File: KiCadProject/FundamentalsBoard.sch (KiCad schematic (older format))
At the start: 17 parts

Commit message: updates
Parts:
- removed P? (x2): CONN_01X02, symbol CONN_01X02
- added C? (x3): 0.1 uF, symbol C
- added P? (x7): CONN_02X02, symbol CONN_02X02
- added P? (x3): CONN_01X03, symbol CONN_01X03
- added R? (x10): 5k, symbol R
- added R? (x3): 10k, symbol R
- added RV? (x2): 5k, symbol POT
- added RV? (x6): 10k, symbol POT
- added U? (x6): MCP601, symbol MCP601
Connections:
- net C_EmitterIn: now also P?.1 (P1), P?.2 (P2)
- net C_EmitterOut: now also P?.3 (P3), P?.4 (P4)
- net GND: now also C?.1, R?.1, R?.1, R?.1, R?.1, R?.2, RV?.3, U?.2 (V-), U?.2 (V-), U?.2 (V-), U?.2 (V-), U?.2 (V-), U?.2 (V-)
- net VCC: now also P?.1 (P1), P?.2 (P2), R?.1, RV?.1, U?.5 (V+), U?.5 (V+), U?.5 (V+), U?.5 (V+), U?.5 (V+), U?.5 (V+)
- net CMirror_n: now reaches Q?.1 (C)
- net CMirror_n: now also P?.3 (P3), P?.4 (P4)
- new net: P?.1 (P1), RV?.1 (x2)
- new net: P?.2 (P2), RV?.2 (x2)
- new net: P?.3 (P3), RV?.3 (x2)
- new net: R?.2, RV?.3, U?.3 (+)
- new net: RV?.2, U?.4 (-)
- new net: P?.1 (P1), P?.2 (P2), P?.3 (P3), R?.1, RV?.2, U?.1
- new net: R?.1, R?.2, U?.3 (+)
- new net: R?.2, R?.2, U?.4 (-)
- new net: C?.2, R?.2, RV?.1
- new net: R?.2, U?.3 (+) (x2)
- new net: C?.1, RV?.2, U?.4 (-)
- new net: C?.2, RV?.3, U?.4 (-)
- new net: R?.1, RV?.1, U?.3 (+)
- new net: R?.2, U?.4 (-)
- new net: R?.1, U?.3 (+)
- new net: R?.1, R?.1, R?.2, U?.4 (-)
- new net Amp_in: P?.1 (P1), P?.2 (P2), R?.2
- new net Amp_out: P?.3 (P3), P?.4 (P4), RV?.2, U?.1
- new net Diff_in: C?.1, P?.1 (P1), P?.2 (P2)
- new net Diff_out: P?.3 (P3), P?.4 (P4), RV?.2, U?.1
- new net Int_in: P?.1 (P1), P?.2 (P2), RV?.3
- new net Int_out: C?.2, P?.3 (P3), P?.4 (P4), U?.1
- new net STrigger_in: P?.1 (P1), P?.2 (P2), RV?.2
- new net STrigger_out: P?.3 (P3), P?.4 (P4), R?.1, U?.1
- new net V1add_in: P?.3 (P3), R?.2
- new net V2add_in: P?.1 (P1), R?.2
- new net Vadd_out: P?.2 (P2), P?.4 (P4), R?.1, U?.1
- no-connect marks 2 -> 7
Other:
- note added: "Amplifier"
- note added: "Differentiator\n"
- note added: "Extra 10k\nPotentiometer"
- note added: "Extra 5k\nPotentiometer"
- note added: "G=-Rf/Rin"
- note added: "Integrator\n"
- note added: "Osc. range:\n1kHz - inf"
- note added: "Schmitt Trigger"
- note added: "Schmitt Trigger\nBased Oscillator\n"
- note added: "Voltage Adder\n"

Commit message: Added Footprints
Added footprint types to most components
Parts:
- removed Q? (x3): BC550, TO-92, symbol BC550
- added D? (x3): LED, LEDs:LED_0603, symbol LED
- added P?: CONN_01X03, Pin_Headers:Pin_Header_Straight_1x03, symbol CONN_01X03
- added R? (x3): 470R, Resistors_SMD:R_0603, symbol R
- C21, C? (x2): footprint (none) -> Capacitors_SMD:C_0603
- C?: value 0.1 uF -> 1 uF; footprint (none) -> Capacitors_SMD:C_0603
- P? (x7): footprint (none) -> Pin_Headers:Pin_Header_Straight_2x02
- P? (x3): footprint (none) -> Pin_Headers:Pin_Header_Straight_1x03
- Q? (x3): footprint TO-92 -> TO_SOT_Packages_SMD:SOT-23
- R21, R22, R23, R24, R? (x15): footprint (none) -> Resistors_SMD:R_0603
- U? (x6): footprint (none) -> TO_SOT_Packages_SMD:SOT-23-5
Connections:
- net GND: now also D?.1 (K), D?.1 (K), D?.1 (K)
- new net: P?.1 (P1), R?.2
- new net: P?.2 (P2), R?.2
- new net: P?.3 (P3), R?.2
- new net: D?.2 (A), R?.1 (x3)
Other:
- note added: "Misc LEDs\n"
- note added: "Osc. range:\n 100 Hz - inf"
- note removed: "Common Collector"
- note removed: "Osc. range:\n1kHz - inf"
- moved on the sheet: P?, RV?

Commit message: Initial export to the board.
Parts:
- added C1: 1 uF, Capacitors_SMD:C_0603, symbol C
- added C2: 0.1 uF, Capacitors_SMD:C_0603, symbol C
- added P3: USB_OTG, TylerCustom:2013499-1, symbol USB_OTG
- RV1, RV10, RV2, RV4, RV5, RV6, RV7, RV8, RV9: renamed from RV?; footprint (none) -> SMD_Packages:POT_SMD
- RV3: renamed from RV2; footprint (none) -> SMD_Packages:POT_SMD
- gave numbers to parts that had none: 44
- renumbered C21 to C3, R24 to R11, R23 to R12, R22 to R7, R21 to R8
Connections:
- net GND: now also C1.1, C2.1, P3.5 (GND)
- net VCC: now also C1.2, C2.2, P3.1 (VCC)
- no-connect marks 7 -> 11

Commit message: Initial layout
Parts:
- RV1, RV10, RV2, RV3, RV4, RV5, RV6, RV7, RV8, RV9: footprint SMD_Packages:POT_SMD -> TylerCustom:ST-4
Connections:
- net VCC: now also R11.1, R7.1
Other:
- moved on the sheet: C3, D1, D2, D3, P10, P11, P12, P9, Q1, R11, R12, R18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

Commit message: Improved layout
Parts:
- added P13: CONN_02X02, Pin_Headers:Pin_Header_Straight_2x02, symbol CONN_02X02
- added R23, R24: 5k, Resistors_SMD:R_0603, symbol R
- R11: value 10k -> 5k
- R12, RV3: value 5k -> 10k
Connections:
- net GND: now also P13.3 (P3), P13.4 (P4), R23.1, R24.1; no longer R15.1, R17.1
- net VCC: now also R12.2, R15.1, R17.1, P13.1 (P1), P13.2 (P2)
- net CE_base: now reaches C3.1, Q1.2 (B), R7.2, R8.1
- net CE_emitter: now reaches Q1.3 (E)
- net CE_emitter: now also RV3.2; no longer R12.2
- net CM_baseCollector: now reaches Q2.1 (C), Q2.2 (B), Q3.2 (B), RV5.3
- net CM_emitterSet: now reaches Q2.3 (E), R14.2
- net CM_emitterMirror: now reaches Q3.3 (E), R16.2
- net at R12.1: now also R21.2, U6.4 (-); no longer RV3.2
- net 5kpot_1: now reaches P12.1 (P1), RV10.1
- net 5kpot_2: now reaches P12.2 (P2), RV10.2
- net 5kpot_3: now reaches P12.3 (P3), RV10.3
- net 10kpot_1: now reaches P11.1 (P1), RV9.1
- net 10kpot_2: now reaches P11.2 (P2), RV9.2
- net 10kpot_3: now reaches P11.3 (P3), RV9.3
- net at R15.2, U4.3 (+): now also R23.2
- net at C5.1, U4.4 (-): no longer RV6.2
- net at R17.2, U5.3 (+): now also R24.2
- net LED1_in: now reaches P9.1 (P1), R18.2
- net LED2_in: now reaches P9.2 (P2), R20.2
- net LED3_in: now reaches P9.3 (P3), R22.2
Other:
- note added: "G = -Rc/Re\n = -R11/RV3\n"
- note added: "Iset = 410 uA - 8.6 mA\n (roughly)\n"
- note removed: "G = -Rc/Re\n = -R24/(R23+RV2)\n"
- moved on the sheet: C1, C2, P3, RV6

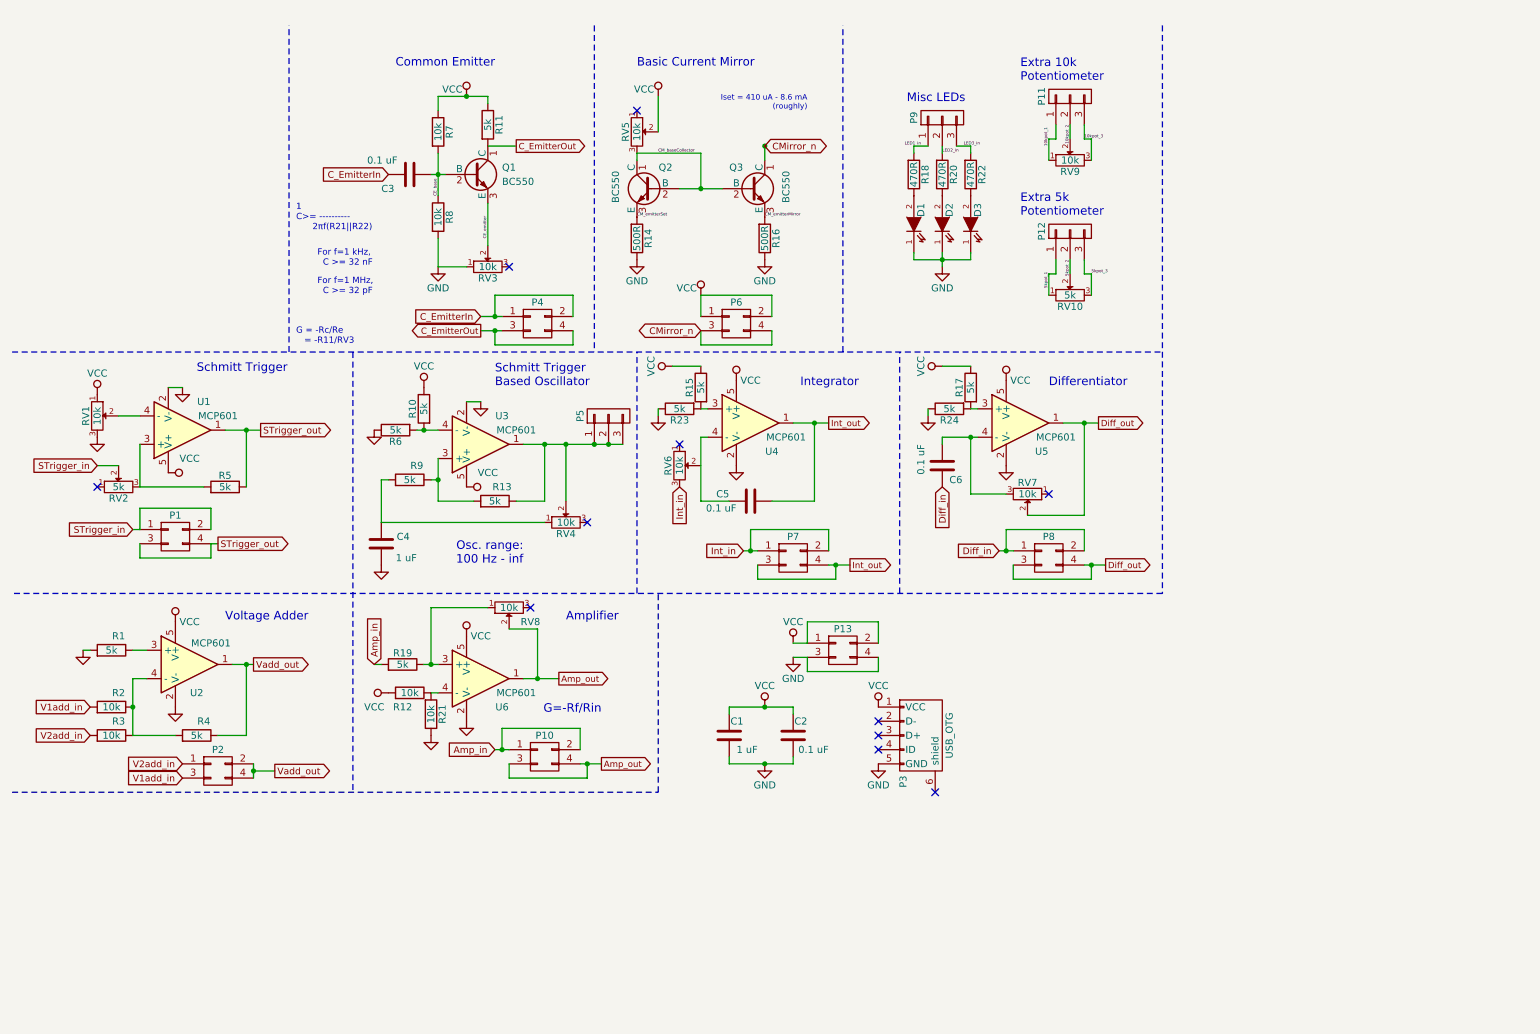
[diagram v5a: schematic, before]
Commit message: Final routing and Gerber export
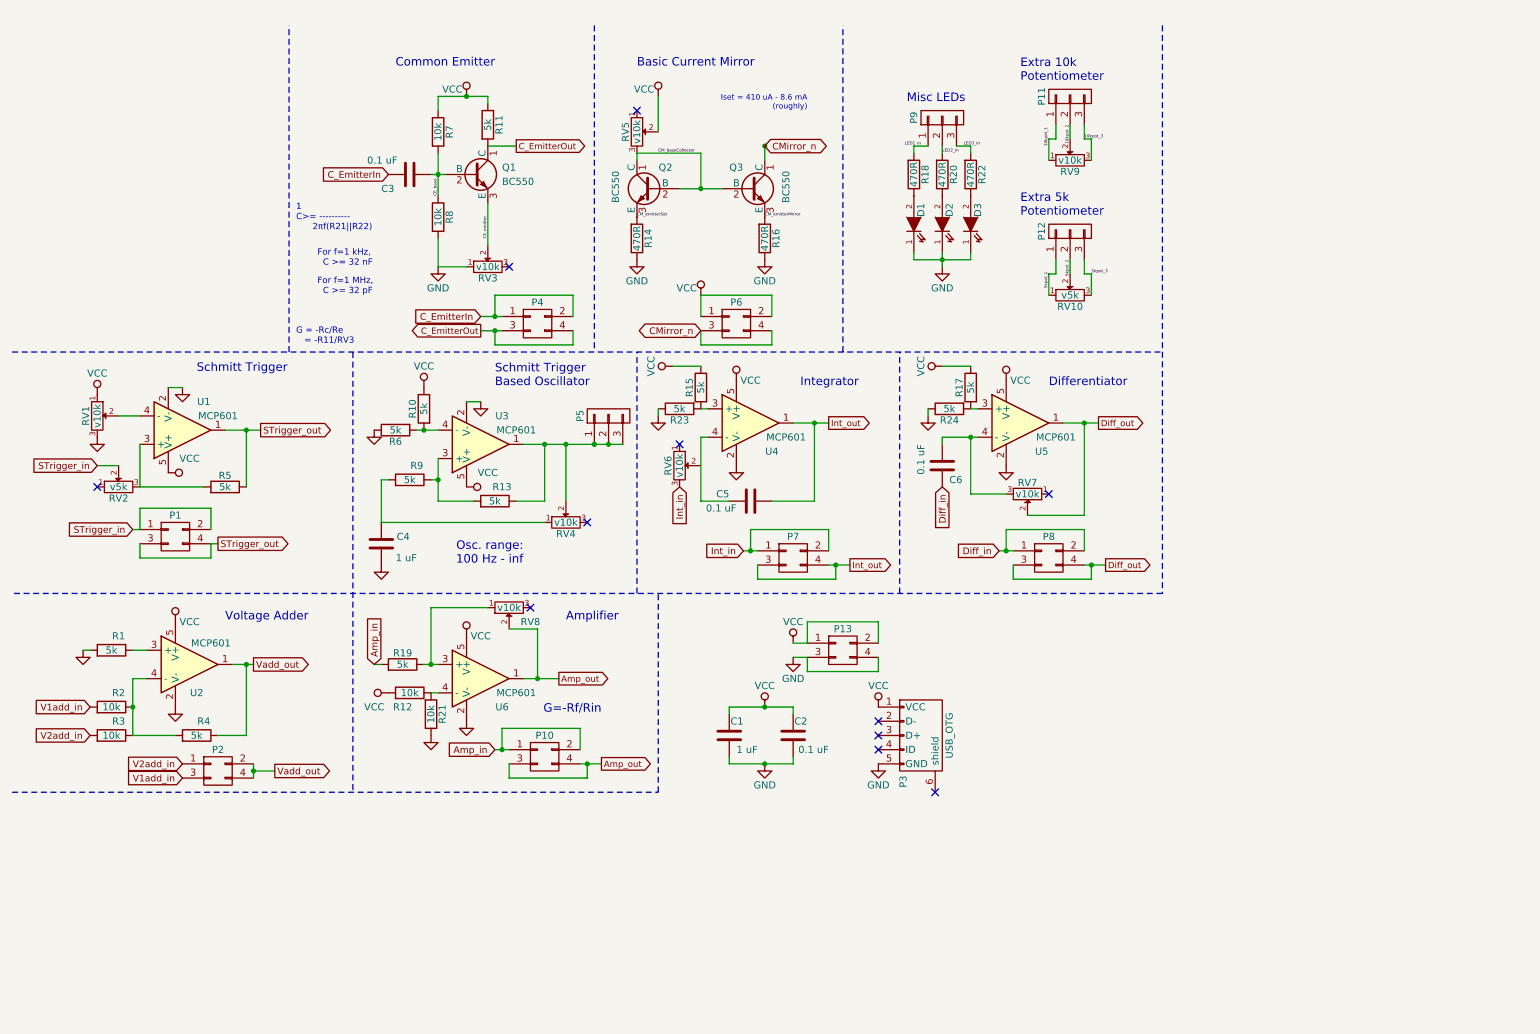
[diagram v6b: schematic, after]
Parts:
- R14, R16: value 500R -> 470R
- RV1, RV3, RV4, RV5, RV6, RV7, RV8, RV9: value 10k -> v10k
- RV10, RV2: value 5k -> v5k
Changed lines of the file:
@@
 P 3850 2200
 F 0 "RV3" H 3850 2120 50  0000 C CNN
-F 1 "10k" H 3850 2200 50  0000 C CNN
+F 1 "v10k" H 3850 2200 50  0000 C CNN
 F 2 "TylerCustom:ST-4" H 3850 2200 50  0001 C CNN
 F 3 "" H 3850 2200 50  0000 C CNN
@@
 P 4900 2000
 F 0 "R14" V 4980 2000 50  0000 C CNN
-F 1 "500R" V 4900 2000 50  0000 C CNN
+F 1 "470R" V 4900 2000 50  0000 C CNN
 F 2 "Resistors_SMD:R_0603" V 4830 2000 50  0001 C CNN
 F 3 "" H 4900 2000 50  0000 C CNN
@@
 P 5800 2000
 F 0 "R16" V 5880 2000 50  0000 C CNN
-F 1 "500R" V 5800 2000 50  0000 C CNN
+F 1 "470R" V 5800 2000 50  0000 C CNN
 F 2 "Resistors_SMD:R_0603" V 5730 2000 50  0001 C CNN
 F 3 "" H 5800 2000 50  0000 C CNN
@@
 P 4900 1250
 F 0 "RV5" H 4900 1170 50  0000 C CNN
-F 1 "10k" H 4900 1250 50  0000 C CNN
+F 1 "v10k" H 4900 1250 50  0000 C CNN
 F 2 "TylerCustom:ST-4" H 4900 1250 50  0001 C CNN
 F 3 "" H 4900 1250 50  0000 C CNN
@@
 P 7950 2400
 F 0 "RV10" H 7950 2320 50  0000 C CNN
-F 1 "5k" H 7950 2400 50  0000 C CNN
+F 1 "v5k" H 7950 2400 50  0000 C CNN
 F 2 "TylerCustom:ST-4" H 7950 2400 50  0001 C CNN
 F 3 "" H 7950 2400 50  0000 C CNN
@@
 P 7950 1450
 F 0 "RV9" H 7950 1370 50  0000 C CNN
-F 1 "10k" H 7950 1450 50  0000 C CNN
+F 1 "v10k" H 7950 1450 50  0000 C CNN
 F 2 "TylerCustom:ST-4" H 7950 1450 50  0001 C CNN
 F 3 "" H 7950 1450 50  0000 C CNN
@@
 P 1250 3750
 F 0 "RV2" H 1250 3670 50  0000 C CNN
-F 1 "5k" H 1250 3750 50  0000 C CNN
+F 1 "v5k" H 1250 3750 50  0000 C CNN
 F 2 "TylerCustom:ST-4" H 1250 3750 50  0001 C CNN
 F 3 "" H 1250 3750 50  0000 C CNN
@@
 P 1100 3250
 F 0 "RV1" H 1100 3170 50  0000 C CNN
-F 1 "10k" H 1100 3250 50  0000 C CNN
+F 1 "v10k" H 1100 3250 50  0000 C CNN
 F 2 "TylerCustom:ST-4" H 1100 3250 50  0001 C CNN
 F 3 "" H 1100 3250 50  0000 C CNN
@@
 P 4400 4000
 F 0 "RV4" H 4400 3920 50  0000 C CNN
-F 1 "10k" H 4400 4000 50  0000 C CNN
+F 1 "v10k" H 4400 4000 50  0000 C CNN
 F 2 "TylerCustom:ST-4" H 4400 4000 50  0001 C CNN
 F 3 "" H 4400 4000 50  0000 C CNN
@@
 P 5200 3600
 F 0 "RV6" H 5200 3520 50  0000 C CNN
-F 1 "10k" H 5200 3600 50  0000 C CNN
+F 1 "v10k" H 5200 3600 50  0000 C CNN
 F 2 "TylerCustom:ST-4" H 5200 3600 50  0001 C CNN
 F 3 "" H 5200 3600 50  0000 C CNN
@@
 P 7650 3800
 F 0 "RV7" H 7650 3720 50  0000 C CNN
-F 1 "10k" H 7650 3800 50  0000 C CNN
+F 1 "v10k" H 7650 3800 50  0000 C CNN
 F 2 "TylerCustom:ST-4" H 7650 3800 50  0001 C CNN
 F 3 "" H 7650 3800 50  0000 C CNN
@@
 P 4000 4600
 F 0 "RV8" H 4150 4700 50  0000 C CNN
-F 1 "10k" H 4000 4600 50  0000 C CNN
+F 1 "v10k" H 4000 4600 50  0000 C CNN
 F 2 "TylerCustom:ST-4" H 4000 4600 50  0001 C CNN
 F 3 "" H 4000 4600 50  0000 C CNN

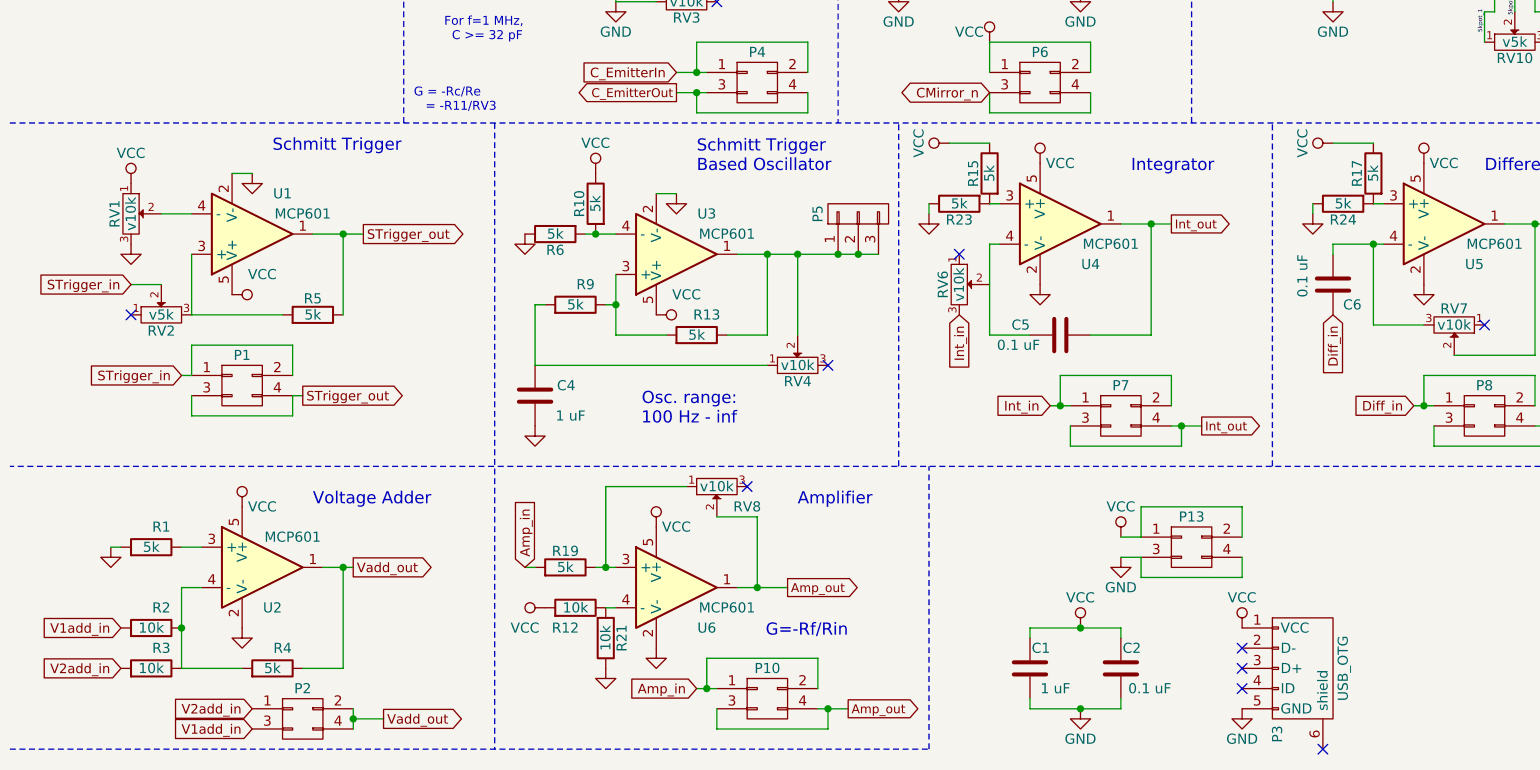
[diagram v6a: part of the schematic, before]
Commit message: Corrected mistake in Amplifier feedback
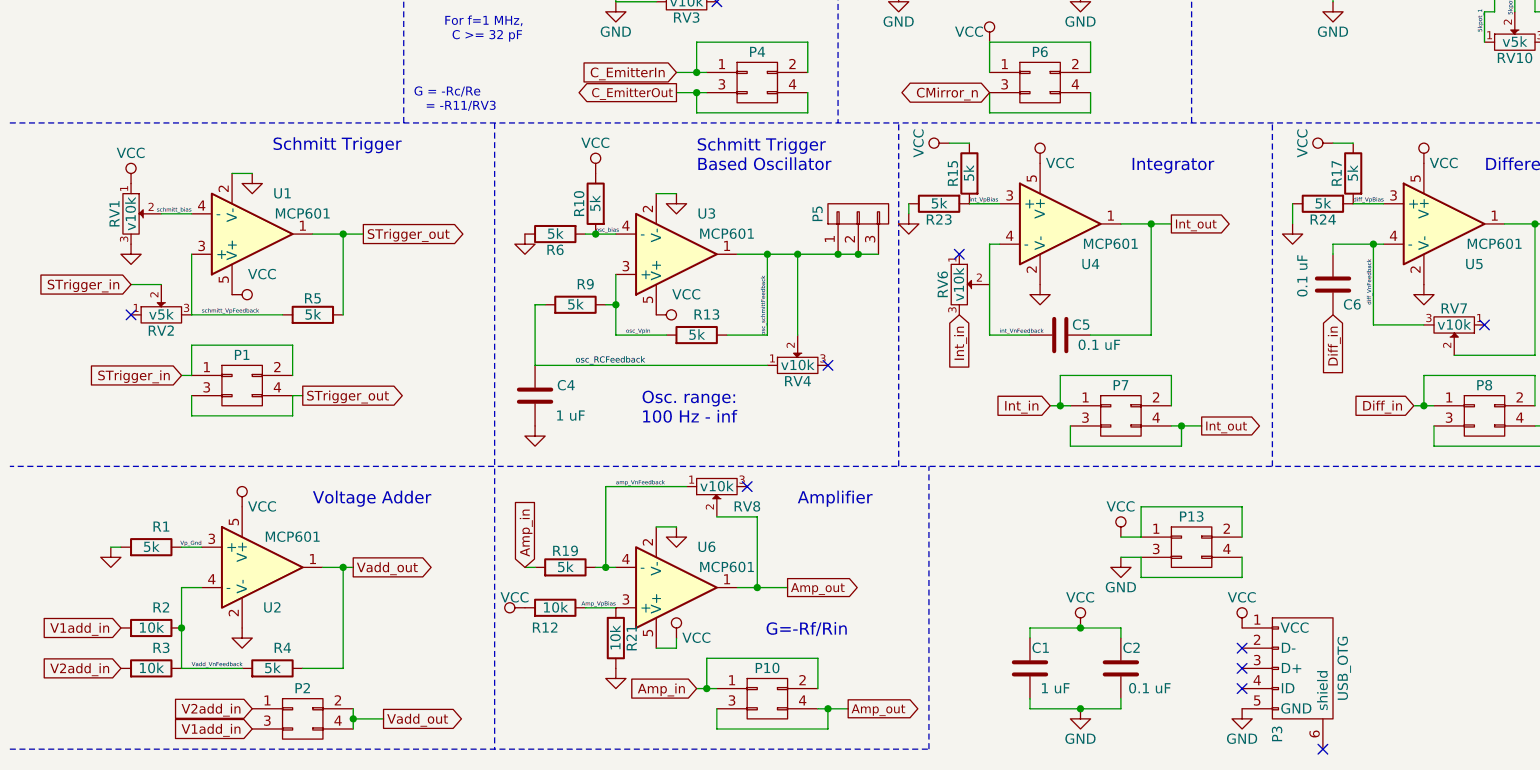
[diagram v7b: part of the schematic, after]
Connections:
- net schmitt_VpFeedback: now reaches R5.2, RV2.3, U1.3 (+)
- net schmitt_bias: now reaches RV1.2, U1.4 (-)
- net osc_schmittFeedback: now reaches P5.1 (P1), P5.2 (P2), P5.3 (P3), R13.1, RV4.2, U3.1
- net osc_VpIn: now reaches R13.2, R9.1, U3.3 (+)
- net osc_bias: now reaches R10.2, R6.2, U3.4 (-)
- net osc_RCFeedback: now reaches C4.2, R9.2, RV4.1
- net int_VpBias: now reaches R15.2, R23.2, U4.3 (+)
- net int_VnFeedback: now reaches C5.1, U4.4 (-)
- net diff_VpBias: now reaches R17.2, R24.2, U5.3 (+)
- net diff_VnFeedback: now reaches C6.2, RV7.3, U5.4 (-)
- net amp_VnFeedback: now reaches R19.1, RV8.1
- net amp_VnFeedback: now also U6.4 (-); no longer U6.3 (+)
- net Amp_VpBias: now reaches R12.1, R21.2
- net Amp_VpBias: now also U6.3 (+); no longer U6.4 (-)
- net Vp_Gnd: now reaches R1.1, U2.3 (+)
- net Vadd_VnFeedback: now reaches R2.1, R3.1, R4.2, U2.4 (-)
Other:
- moved on the sheet: R12, R15, R17, R21, R23, R24
